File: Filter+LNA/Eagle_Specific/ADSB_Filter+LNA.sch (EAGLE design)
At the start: 12 parts, among them U1 BFP420, X1 SMA-142-0701-801/806, X2 SMA-142-0701-801/806

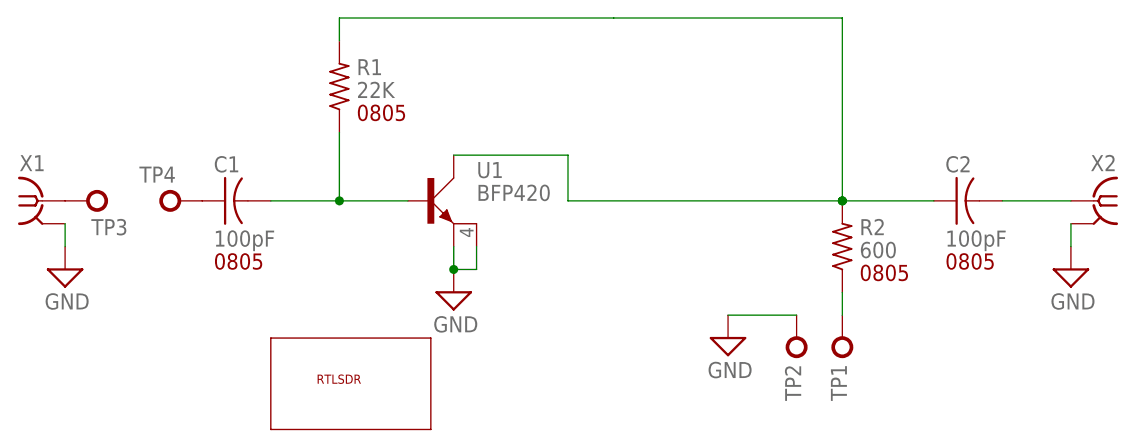
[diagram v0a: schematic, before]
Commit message: Minor changes to Filter+LNA Layout
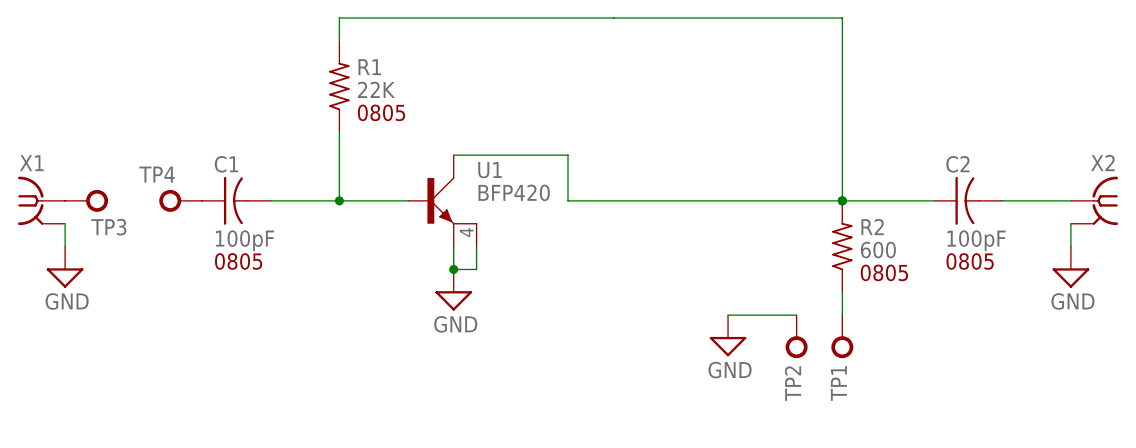
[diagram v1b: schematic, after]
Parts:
- removed U$1: RTLSDR-LARGE, logos:RTLSDR-LARGE
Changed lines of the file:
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@@
 <part name="TP3" library="Pads_Test_Points" deviceset="TEST_POINT" device="S8_8"/>
 <part name="TP4" library="Pads_Test_Points" deviceset="TEST_POINT" device="S8_8"/>
-<part name="U$1" library="logos" deviceset="RTLSDR-LARGE" device=""/>
 </parts>
 <sheets>
@@
 <attribute name="NAME" x="108.839" y="123.19" size="1.778" layer="95" rot="R180"/>
 </instance>
-<instance part="U$1" gate="G$1" x="119.38" y="93.98"/>
 </instances>
 <busses>
